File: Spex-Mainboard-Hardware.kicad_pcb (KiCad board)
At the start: 4 copper layers, 82 x 84.7 mm, 121 parts, among them P1 USB_OTG, P13 CONN_01X02, P14 CONN_01X02, P3 CONN_01X04, P4 CONN_01X04, P5 CONN_01X04, P6 CONN_01X04, P7 CONN_01X02, P8 CONN_01X02, P9 CONN_01X02, Q105 Si3407DV, Q106 Q_PNP_BEC, Q3 BSS215PH6327, Q4 Si5468DC, Q5 Si5468DC, Q6 Si5468DC, SW1 SW_PUSH, SW2 SW_PUSH, U1 MKL02Z32VFG4, U10 LM4030, U105 TPS563200, U108 TPS563200, U12 ST1480ABDR, U13 SCHA4B0419, U14 AT45DB641E, U2 NUP2201MR6, U3 MK20DX256VLH7, U4 NUP2201MR6, U5 NUP2201MR6, U6 MMQA6V2T1G, U7 MCP9808T, U8 BME280, U9 LSM9DS1, Y1 Crystal

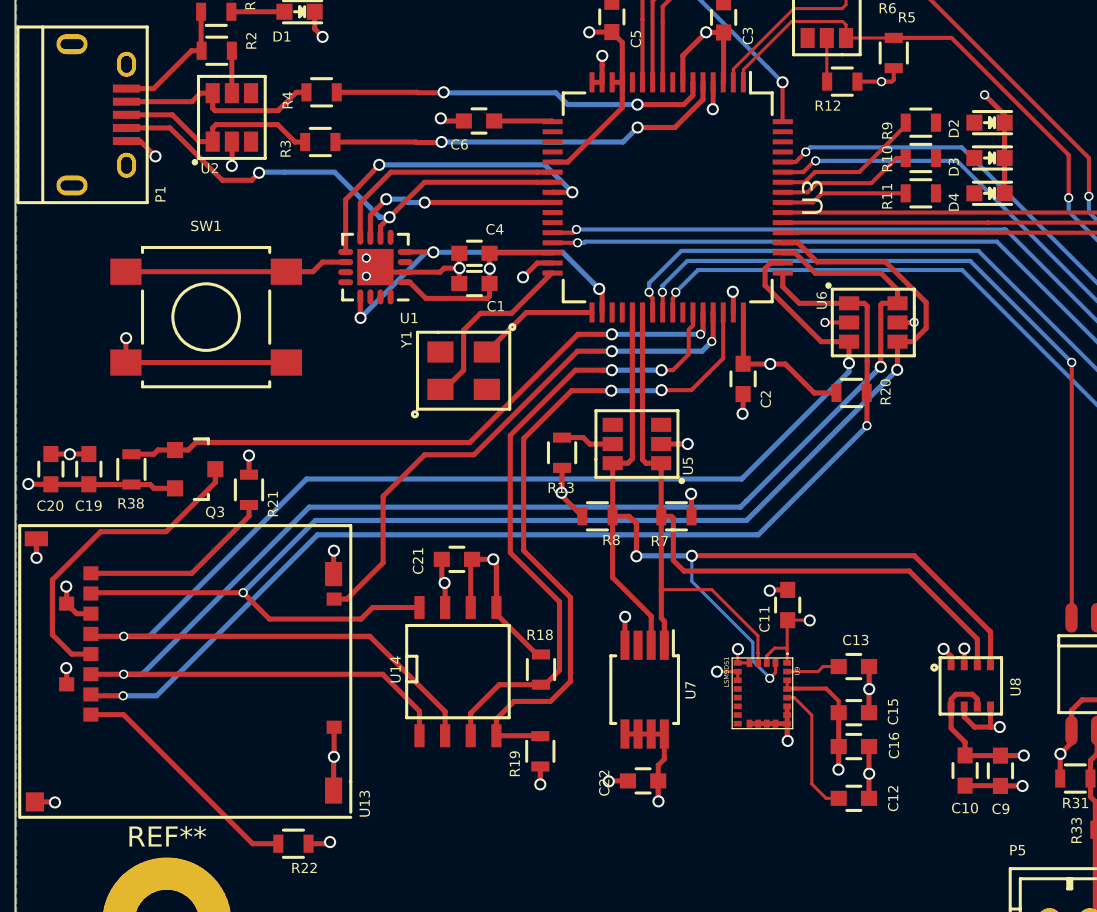
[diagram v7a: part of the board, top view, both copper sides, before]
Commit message: removed SPI Flash, minor changes, updated Kicad
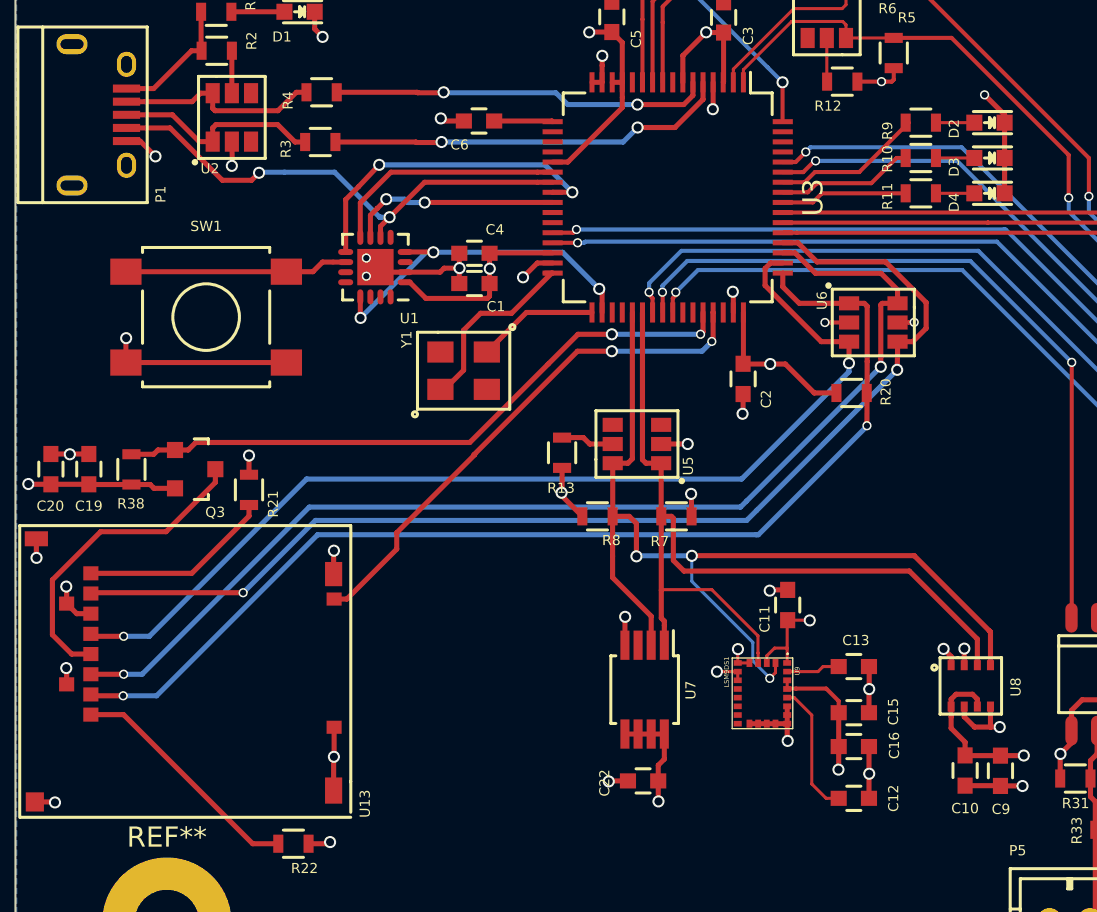
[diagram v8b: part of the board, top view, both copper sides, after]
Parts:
- removed C21: 1uF, Capacitors_SMD:C_0603
- removed R18, R19: 10K, Resistors_SMD:R_0603
- removed U14: AT45DB641E, SMD_Packages:SOIC-8-N
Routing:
- net SPI0_CS1: track 34.2 -> 0.00 mm, vias 2 -> 0
- net Flash_Reset: track 31.7 -> 0.00 mm, vias 2 -> 0
- net SPI0_SCK: track 70.3 -> 51.7 mm
- net SPI0_MOSI: track 73.1 -> 56.5 mm
- net +3V3: track 108.6 -> 98.4 mm, vias 24 -> 22
- net SPI0_MISO: track 66.7 -> 57.2 mm
- net GND: track 134.8 -> 132.4 mm, vias 60 -> 59
- net Net-(D4-Pad2): track 0.00 -> 1.90 mm
- net Net-(D3-Pad2): track 0.00 -> 1.90 mm
- net Net-(D2-Pad2): track 0.00 -> 1.90 mm
- net SD_Detect: track 27.4 -> 26.0 mm
